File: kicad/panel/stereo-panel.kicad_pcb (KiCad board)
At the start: 2 copper layers, 144.1 x 144.1 mm, 347 parts, among them J1 AC IN 12-15V, J1 DC 12V IN, J1 IN L-G-R, J2 DC IN 12V, J2 IN L-G-R, J2 OUT L-G-R, J3 DC OUT 1, J3 LED IN, J3 SPK L, J4 DC OUT 2, J4 SPK R, J5 LED REMOTE, Q1 BC547, Q1001 BC547, Q1002 BC547, Q1003 BC557, Q1004 BD139, Q1005 BD140, Q1006 BC547, Q2 TIP41C, Q2001 BC547, Q2002 BC547, Q2003 BC557, Q2004 BD139, Q2005 BD140, Q2006 BC547, Q3 BC547

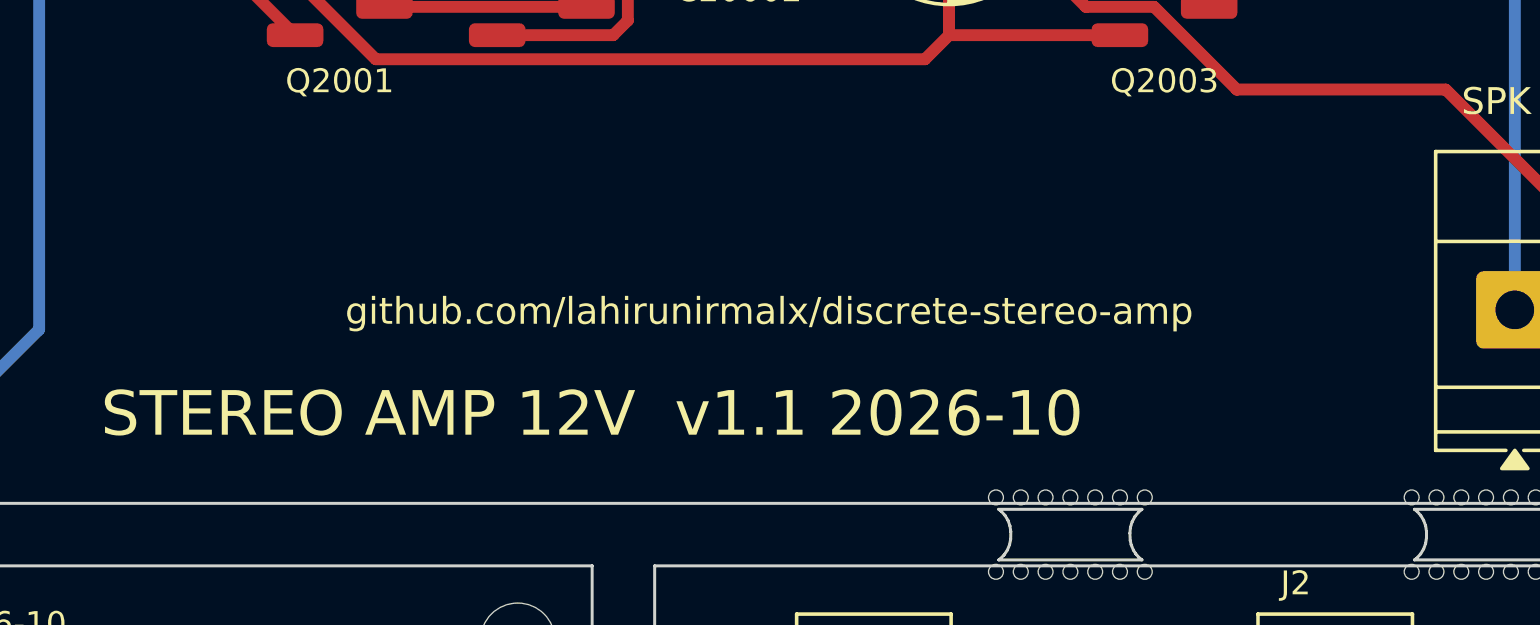
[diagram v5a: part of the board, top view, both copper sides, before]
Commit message: Compact 100 x 85 mm amp layout as a selectable second variant; modular build paths and the three design rules documented; per-board gerbers include both amps
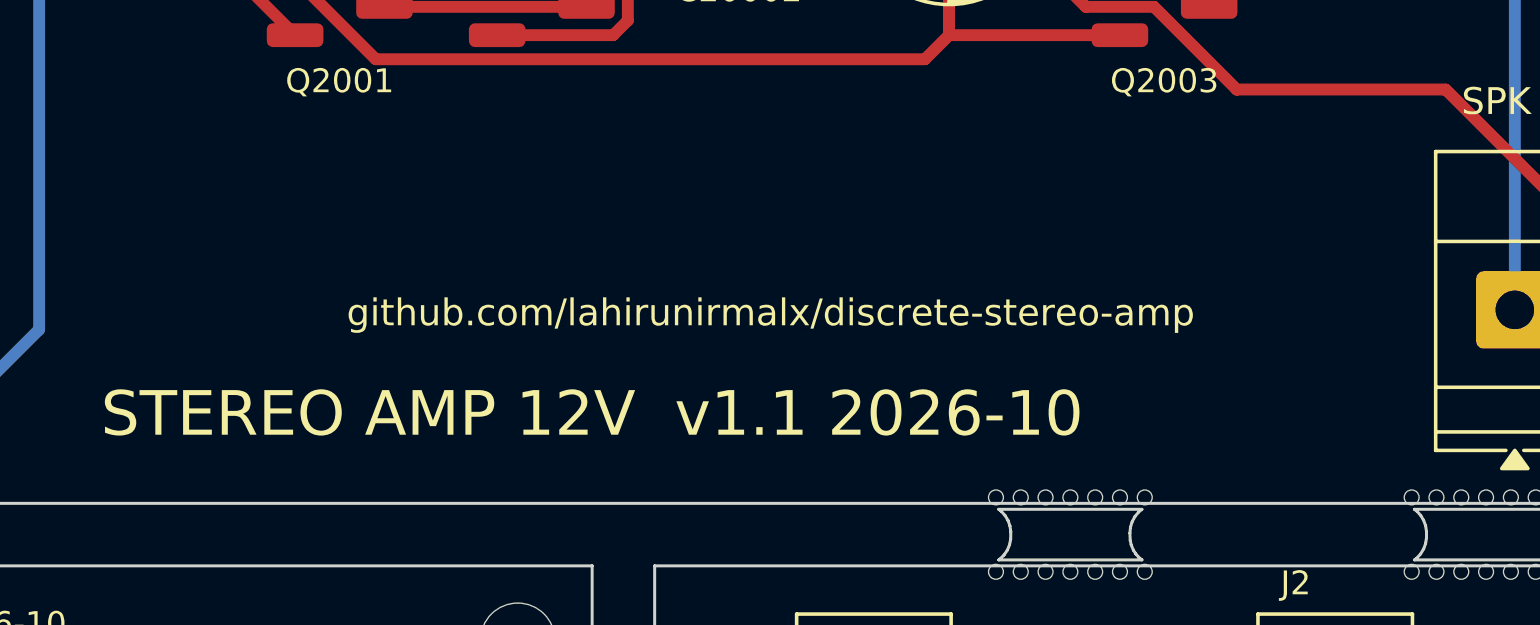
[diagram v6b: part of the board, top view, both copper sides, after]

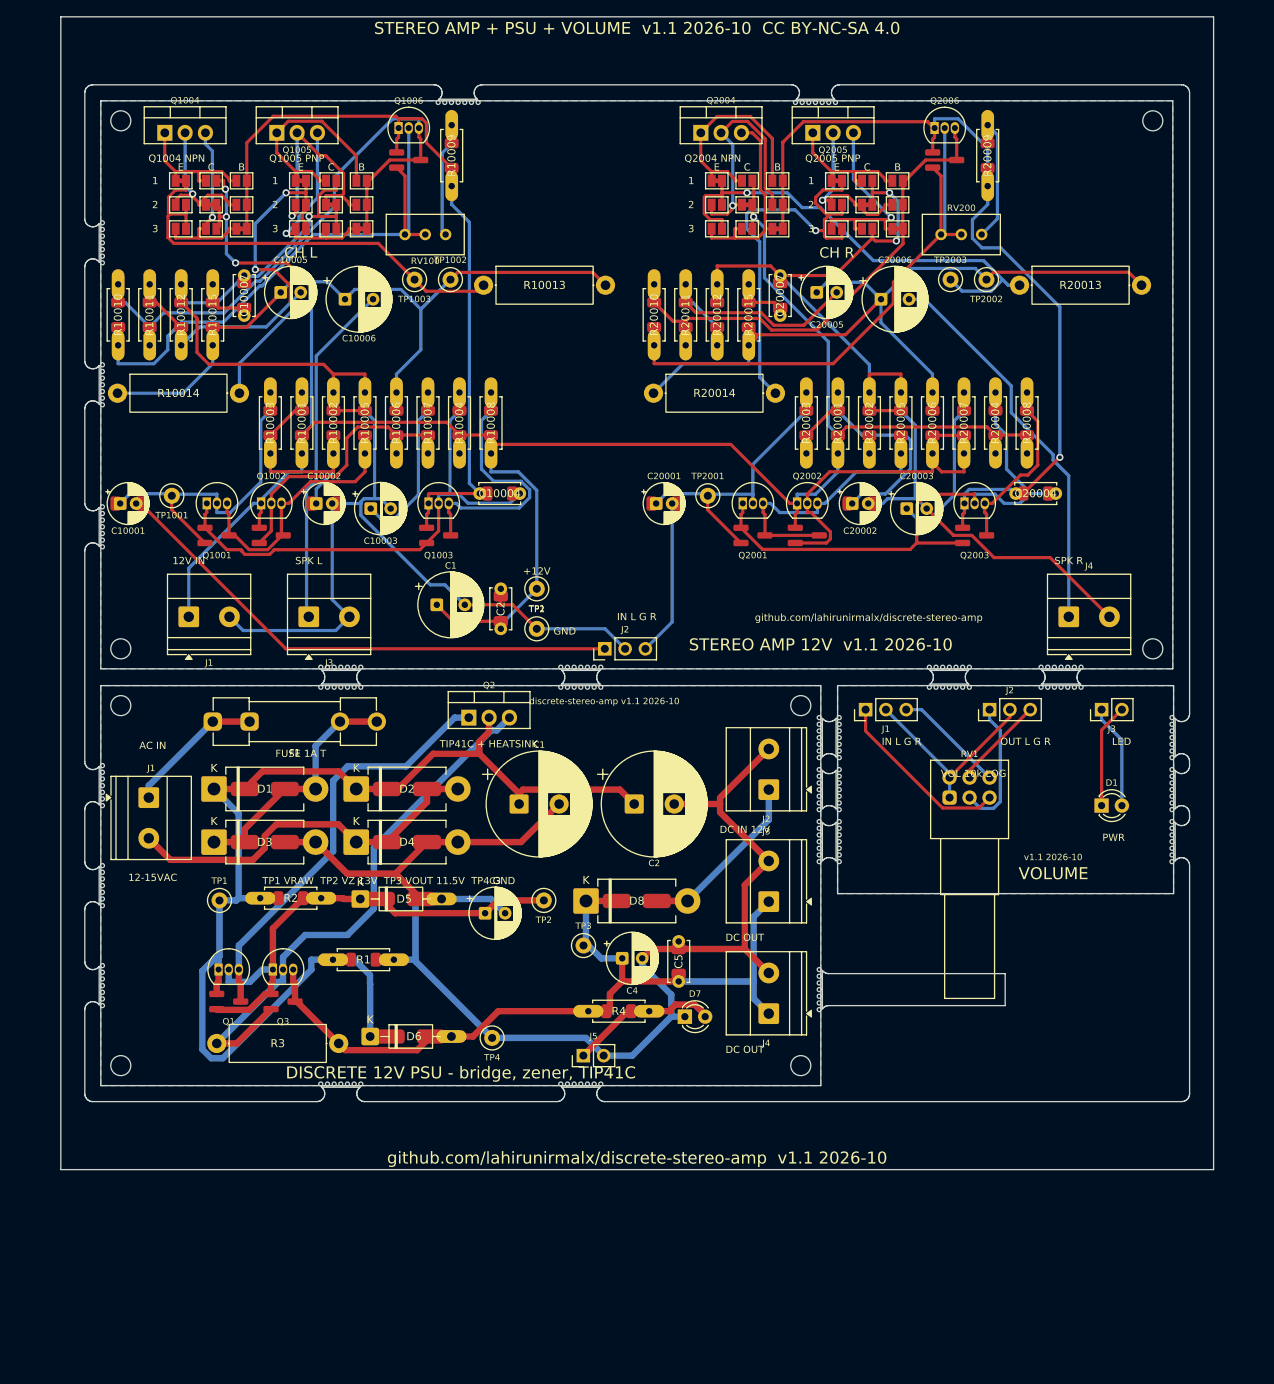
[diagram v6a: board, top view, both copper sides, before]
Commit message: Release 1.2: mirror-loaded front end, closed-loop PSU, VU tap, headphone board
- Amp: PNP input pair with NPN current-mirror load, LED-referenced current-source tail,
  NPN VAS with bootstrapped load from +12V, 220p Miller + 47p lead cap (THD 0.004% at 26 mW/8R,
  0.019% at 0.29 W; was 0.03 / 0.2). 1k VU meter tap per channel to header J5.
- PSU: BC547 error amplifier, 5.6 V zener fed from VOUT, 8.2k + 2k trimmer / 10k divider,
  2.2k drive, 47n/100n compensation. 12.0 V set point, 0.14 V dip on a 1 A step.
- New headphone board (DPDT switch, 120R series, DIRECT jumpers, 3.5 mm jack, panel-jack header).
- Boards: amp 134x85 / compact 100x98, PSU 90x58, hp 42x30; panel 155x155 with four boards.
  All 2-layer boards and the panel DRC clean; single-sided amp down to 15 errors.
- Toolchain: STAMP constant, reroute.sh second routing pass, rotated titles, link holes on
  jumper pads, 2 mm routing corridor per channel.
- Docs, BOMs, order guide, changelog, known issues rewritten for release 2.
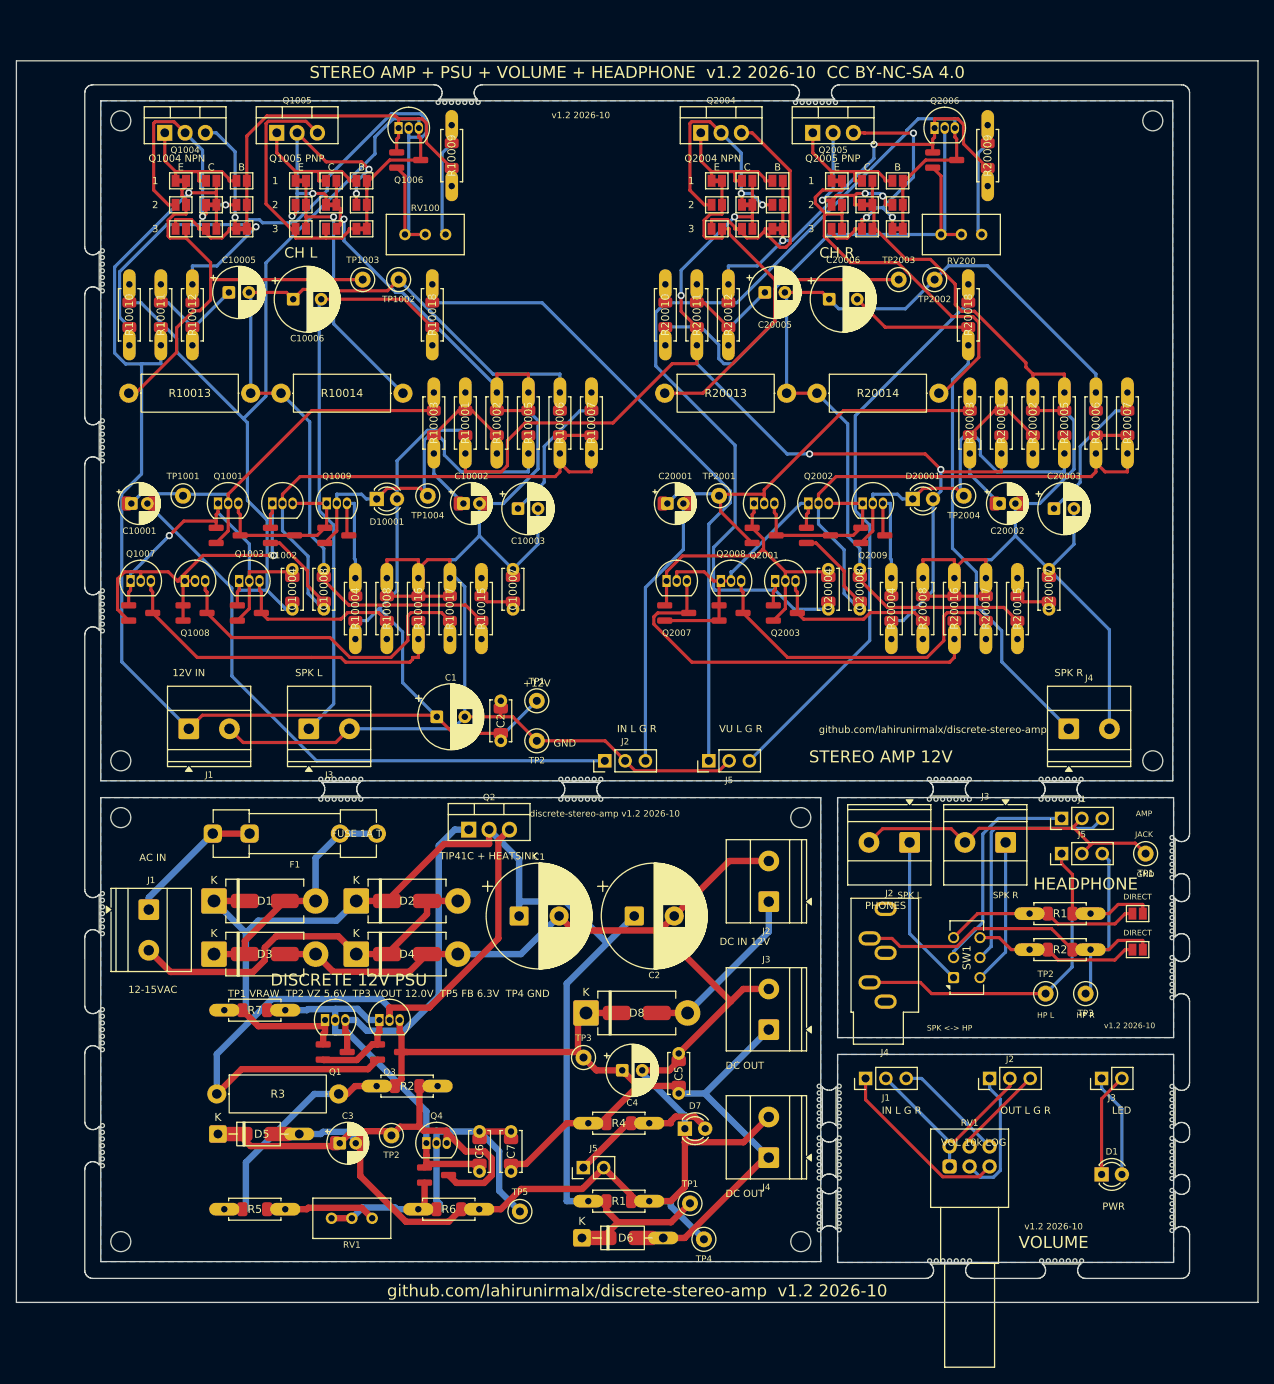
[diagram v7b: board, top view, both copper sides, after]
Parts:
- removed the C1 at (42.0, 63.0)
- removed the C1 at (52.3, 87.9)
- removed the C2 at (50.0, 66.0)
- removed the C2 at (66.7, 87.9)
- removed the D1 at (14.2, 86.0)
- removed the D1 at (125.1, 88.1)
- removed the H3 at (2.50, 68.5)
- removed the H3 at (2.50, 120.6)
- removed the H4 at (131.5, 68.5)
- removed the H4 at (87.5, 120.6)
- removed the J1 at (6.00, 87.1)
- removed the J1 at (95.6, 76.1)
- removed the J1 at (11.0, 64.5)
- removed the J2 at (63.0, 68.5)
- removed the J2 at (83.5, 86.1)
- removed the J2 at (111.1, 76.1)
- removed the J3 at (26.0, 64.5)
- removed the J3 at (125.1, 76.1)
- removed the J3 at (83.5, 100.1)
- removed the J4 at (83.5, 114.1)
- removed the J4 at (121.0, 64.5)
- removed the J5 at (60.3, 119.3)
- removed the R1 at (29.0, 107.4)
- removed the R2 at (19.9, 99.7)
- removed the RV1 at (106.1, 87.1)
- removed the TP1 at (54.5, 61.0)
- removed the TP1 at (14.8, 100.0)
- removed the TP2 at (54.5, 66.0)
- removed the TP2 at (55.4, 100.0)
- removed the TP3 at (60.3, 105.6)
- added C1: 1000u, Capacitor_THT:CP_Radial_D8.0mm_P3.50mm, F.Cu at (42.0, 77.0)
- added C1: 2200u, Capacitor_THT:CP_Radial_D13.0mm_P5.00mm, F.Cu at (52.3, 101.9)
- added C10008: 47p, Custom:C_P5_1206, F.Cu at (27.9, 63.6)
- added C2: 100n, Custom:C_P5_1206, F.Cu at (50.0, 80.0)
- added C2: 2200u, Capacitor_THT:CP_Radial_D13.0mm_P5.00mm, F.Cu at (66.7, 101.9)
- added C20008: 47p, Custom:C_P5_1206, F.Cu at (94.9, 63.6)
- added C6: 47n, Custom:C_P5_1206, F.Cu at (47.3, 133.8)
- added C7: 100n, Custom:C_P5_1206, F.Cu at (51.3, 133.8)
- added D1: POWER LED, LED_THT:LED_D3.0mm, F.Cu at (125.1, 134.2)
- added D1: 1N5401, Custom:D_DO201_SMA, F.Cu at (14.2, 100.0)
- added D10001: LED red, LED_THT:LED_D3.0mm, F.Cu at (34.5, 49.8)
- added D20001: LED red, LED_THT:LED_D3.0mm, F.Cu at (101.5, 49.8)
- added H3: M2.5, Custom:Hole_2.5mm, F.Cu at (2.50, 142.6)
- added H3: M2.5, Custom:Hole_2.5mm, F.Cu at (2.50, 82.5)
- added H4: M2.5, Custom:Hole_2.5mm, F.Cu at (131.5, 82.5)
- added H4: M2.5, Custom:Hole_2.5mm, F.Cu at (87.5, 142.6)
- added J1: AC IN 12-15V, TerminalBlock_Phoenix:TerminalBlock_Phoenix_MKDS-1,5-2-5.08_1x02_P5.08mm_Horizontal, F.Cu at (6.00, 101.1)
- added J1: IN L-G-R, Connector_PinHeader_2.54mm:PinHeader_1x03_P2.54mm_Vertical, F.Cu at (95.6, 122.2)
- added J1: DC 12V IN, TerminalBlock_Phoenix:TerminalBlock_Phoenix_MKDS-1,5-2-5.08_1x02_P5.08mm_Horizontal, F.Cu at (11.0, 78.5)
- added J1: FROM AMP L-G-R, Connector_PinHeader_2.54mm:PinHeader_1x03_P2.54mm_Vertical, F.Cu at (120.1, 89.7)
- added J2: IN L-G-R, Connector_PinHeader_2.54mm:PinHeader_1x03_P2.54mm_Vertical, F.Cu at (63.0, 82.5)
- added J2: DC IN 12V, TerminalBlock_Phoenix:TerminalBlock_Phoenix_MKDS-1,5-2-5.08_1x02_P5.08mm_Horizontal, F.Cu at (83.5, 100.1)
- added J2: SPK L, TerminalBlock_Phoenix:TerminalBlock_Phoenix_MKDS-1,5-2-5.08_1x02_P5.08mm_Horizontal, F.Cu at (101.1, 92.7)
- added J2: OUT L-G-R, Connector_PinHeader_2.54mm:PinHeader_1x03_P2.54mm_Vertical, F.Cu at (111.1, 122.2)
- added J3: SPK R, TerminalBlock_Phoenix:TerminalBlock_Phoenix_MKDS-1,5-2-5.08_1x02_P5.08mm_Horizontal, F.Cu at (113.1, 92.7)
- added J3: LED IN, Connector_PinHeader_2.54mm:PinHeader_1x02_P2.54mm_Vertical, F.Cu at (125.1, 122.2)
- added J3: SPK L, TerminalBlock_Phoenix:TerminalBlock_Phoenix_MKDS-1,5-2-5.08_1x02_P5.08mm_Horizontal, F.Cu at (26.0, 78.5)
- added J3: DC OUT 1, TerminalBlock_Phoenix:TerminalBlock_Phoenix_MKDS-1,5-2-5.08_1x02_P5.08mm_Horizontal, F.Cu at (83.5, 116.1)
- added J4: SPK R, TerminalBlock_Phoenix:TerminalBlock_Phoenix_MKDS-1,5-2-5.08_1x02_P5.08mm_Horizontal, F.Cu at (121.0, 78.5)
- added J4: 3.5mm TRS, Connector_Audio:Jack_3.5mm_CUI_SJ1-3535NG_Horizontal, F.Cu at (98.1, 112.6)
- added J4: DC OUT 2, TerminalBlock_Phoenix:TerminalBlock_Phoenix_MKDS-1,5-2-5.08_1x02_P5.08mm_Horizontal, F.Cu at (83.5, 132.1)
- added J5: LED REMOTE, Connector_PinHeader_2.54mm:PinHeader_1x02_P2.54mm_Vertical, F.Cu at (60.3, 133.3)
- added J5: PANEL JACK T-G-R, Connector_PinHeader_2.54mm:PinHeader_1x03_P2.54mm_Vertical, F.Cu at (120.1, 94.1)
- added J5: VU L-G-R, Connector_PinHeader_2.54mm:PinHeader_1x03_P2.54mm_Vertical, F.Cu at (76.0, 82.5)
- added JP1: DIRECT, Jumper:SolderJumper-2_P1.3mm_Open_Pad1.0x1.5mm, F.Cu at (129.6, 101.6)
- added JP2: DIRECT, Jumper:SolderJumper-2_P1.3mm_Open_Pad1.0x1.5mm, F.Cu at (129.6, 106.1)
- added KiKit_MB_29_1: NPTH, NPTH, F.Cu at (108.6, 145.0)
- added KiKit_MB_29_2: NPTH, NPTH, F.Cu at (107.8, 145.0)
- added KiKit_MB_29_3: NPTH, NPTH, F.Cu at (106.9, 145.0)
- added KiKit_MB_29_4: NPTH, NPTH, F.Cu at (106.1, 145.0)
- added KiKit_MB_29_5: NPTH, NPTH, F.Cu at (105.3, 145.0)
- added KiKit_MB_29_6: NPTH, NPTH, F.Cu at (104.4, 145.0)
- added KiKit_MB_29_7: NPTH, NPTH, F.Cu at (103.6, 145.0)
- added KiKit_MB_30_1: NPTH, NPTH, F.Cu at (122.6, 145.0)
- added KiKit_MB_30_2: NPTH, NPTH, F.Cu at (121.8, 145.0)
- added KiKit_MB_30_3: NPTH, NPTH, F.Cu at (120.9, 145.0)
- added KiKit_MB_30_4: NPTH, NPTH, F.Cu at (120.1, 145.0)
- added KiKit_MB_30_5: NPTH, NPTH, F.Cu at (119.3, 145.0)
- added KiKit_MB_30_6: NPTH, NPTH, F.Cu at (118.4, 145.0)
- added KiKit_MB_30_7: NPTH, NPTH, F.Cu at (117.6, 145.0)
- added Q1007: BC547, Custom:TO92_SOT23, F.Cu at (3.72, 60.0)
- added Q1008: BC547, Custom:TO92_SOT23, F.Cu at (10.5, 60.0)
- added Q1009: BC557, Custom:TO92_SOT23, F.Cu at (28.2, 50.3)
- added Q2007: BC547, Custom:TO92_SOT23, F.Cu at (70.7, 60.0)
- added Q2008: BC547, Custom:TO92_SOT23, F.Cu at (77.5, 60.0)
- added Q2009: BC557, Custom:TO92_SOT23, F.Cu at (95.2, 50.3)
- added Q4: BC547, Custom:TO92_SOT23, F.Cu at (40.7, 130.3)
- added R1: 120, Custom:R_Axial_1206, F.Cu at (116.1, 101.6)
- added R1: 4.7k, Custom:R_Axial_1206, F.Cu at (60.9, 137.5)
- added R10016: 100, Custom:R_Axial_1206, F.Cu at (39.7, 67.3)
- added R10017: 100, Custom:R_Axial_1206, F.Cu at (43.6, 67.3)
- added R10018: 1k, Custom:R_Axial_1206, F.Cu at (41.4, 30.6)
- added R2: 1k, Custom:R_Axial_1206, F.Cu at (34.5, 123.2)
- added R2: 120, Custom:R_Axial_1206, F.Cu at (116.1, 106.1)
- added R20016: 100, Custom:R_Axial_1206, F.Cu at (106.7, 67.3)
- added R20017: 100, Custom:R_Axial_1206, F.Cu at (110.6, 67.3)
- added R20018: 1k, Custom:R_Axial_1206, F.Cu at (108.4, 30.6)
- added R5: 8.2k, Custom:R_Axial_1206, F.Cu at (15.4, 138.6)
- added R6: 10k, Custom:R_Axial_1206, F.Cu at (39.7, 138.6)
- added R7: 2.2k, Custom:R_Axial_1206, F.Cu at (15.4, 113.7)
- added RV1: 10k log dual, Potentiometer_THT:Potentiometer_Alps_RK097_Dual_Horizontal, F.Cu at (106.1, 133.2)
- added RV1: 2k, Potentiometer_THT:Potentiometer_Bourns_3296W_Vertical, F.Cu at (33.9, 139.7)
- added SW1: SPK / HP, Button_Switch_THT:SW_CK_JS202011CQN_DPDT_Straight, F.Cu at (106.6, 109.6)
- added TP1: +12V, TestPoint:TestPoint_Loop_D2.50mm_Drill1.0mm, F.Cu at (54.5, 75.0)
- added TP1: GND, TestPoint:TestPoint_Loop_D2.50mm_Drill1.0mm, F.Cu at (130.6, 94.1)
- added TP1: VRAW 14-19V, TestPoint:TestPoint_Loop_D2.50mm_Drill1.0mm, F.Cu at (73.7, 137.8)
- added TP1004: LED 10.2V, TestPoint:TestPoint_Loop_D2.50mm_Drill1.0mm, F.Cu at (40.9, 49.4)
- added TP2: VZ 5.6V, TestPoint:TestPoint_Loop_D2.50mm_Drill1.0mm, F.Cu at (36.3, 129.3)
- added TP2: HP L, TestPoint:TestPoint_Loop_D2.50mm_Drill1.0mm, F.Cu at (118.1, 111.6)
- added TP2: GND, TestPoint:TestPoint_Loop_D2.50mm_Drill1.0mm, F.Cu at (54.5, 80.0)
- added TP2004: LED 10.2V, TestPoint:TestPoint_Loop_D2.50mm_Drill1.0mm, F.Cu at (107.9, 49.4)
- added TP3: HP R, TestPoint:TestPoint_Loop_D2.50mm_Drill1.0mm, F.Cu at (123.1, 111.6)
- added TP3: VOUT 12.0V, TestPoint:TestPoint_Loop_D2.50mm_Drill1.0mm, F.Cu at (60.3, 119.6)
- added TP5: FB 6.3V, TestPoint:TestPoint_Loop_D2.50mm_Drill1.0mm, F.Cu at (52.4, 138.8)
- C10004, C20004: value 100p -> 220p
- C3: value 100u -> 10u; footprint Capacitor_THT:CP_Radial_D6.3mm_P2.50mm -> Custom:CE_P2_1206
- D5: value 13V 1W -> 5.6V
- Q1001, Q1002, Q2001, Q2002: value BC547 -> BC557
- Q1003, Q2003: value BC557 -> BC547
- R10004, R20004: value 4.7k -> 1.2k
- R10005, R20005: value 10k -> 4.7k
- TP1001, TP2001: value B1 5.9V -> B1 6.1V
- moved KiKit_MB_19_7 108.0 mm to (133.9, 104.6)
- moved KiKit_MB_19_6 107.3 mm to (133.9, 103.8)
- moved KiKit_MB_19_5 106.6 mm to (133.9, 102.9)
- moved KiKit_MB_19_4 106.0 mm to (133.9, 102.1)
- moved KiKit_MB_19_3 105.3 mm to (133.9, 101.3)
- moved KiKit_MB_19_2 104.7 mm to (133.9, 100.4)
- moved KiKit_MB_19_1 104.0 mm to (133.9, 99.6)
- moved KiKit_MB_18_1 78.7 mm to (133.9, 92.1)
- moved KiKit_MB_18_2 78.1 mm to (133.9, 92.9)
- moved KiKit_MB_18_3 77.5 mm to (133.9, 93.8)
- moved KiKit_MB_20_7 77.2 mm to (133.9, 112.1)
- moved KiKit_MB_18_4 76.9 mm to (133.9, 94.6)
- moved KiKit_MB_20_6 76.5 mm to (133.9, 111.3)
- moved KiKit_MB_18_5 76.3 mm to (133.9, 95.4)
- moved KiKit_MB_18_6 75.8 mm to (133.9, 96.3)
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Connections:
- C10004 pad 1: Board_0-/VAS_L -> Board_0-/B5_L
- C10004 pad 1S: Board_0-/VAS_L -> Board_0-/B5_L
- C10005 pad 1: Board_0-/OUT_L -> Board_0-Net-(C10005-Pad1)
- C10005 pad 2: Board_0-Net-(C10005-Pad2) -> Board_0-/OUT_L
- C20004 pad 1: Board_0-/VAS_R -> Board_0-/B5_R
- C20004 pad 1S: Board_0-/VAS_R -> Board_0-/B5_R
- C20005 pad 1: Board_0-/OUT_R -> Board_0-Net-(C20005-Pad1)
- C20005 pad 2: Board_0-Net-(C20005-Pad2) -> Board_0-/OUT_R
- C3 pad 1: Board_1-/VZ -> Board_1-Net-(D5-K)
- D5 pad 1: Board_1-/VZ -> Board_1-Net-(D5-K)
- D5 pad 1S: Board_1-/VZ -> Board_1-Net-(D5-K)
- Q1 pad 2: Board_1-/VZ -> Board_1-/BQ1
- Q1 pad 2S: Board_1-/VZ -> Board_1-/BQ1
- Q1002 pad 1: Board_0-+12V -> Board_0-Net-(Q1002-C)
- Q1002 pad 1S: Board_0-+12V -> Board_0-Net-(Q1002-C)
- Q1003 pad 1: Board_0-/VAS_L -> Board_0-/B5_L
- Q1003 pad 1S: Board_0-/VAS_L -> Board_0-/B5_L
- Q2002 pad 1: Board_0-+12V -> Board_0-Net-(Q2002-C)
- Q2002 pad 1S: Board_0-+12V -> Board_0-Net-(Q2002-C)
- Q2003 pad 1: Board_0-/VAS_R -> Board_0-/B5_R
- Q2003 pad 1S: Board_0-/VAS_R -> Board_0-/B5_R
- Q3 pad 1: Board_1-/VZ -> Board_1-/BQ1
- Q3 pad 1S: Board_1-/VZ -> Board_1-/BQ1
- R10004 pad 2: Board_0-Net-(Q1001-C) -> Board_0-Net-(Q1009-E)
- R10004 pad 2S: Board_0-Net-(Q1001-C) -> Board_0-Net-(Q1009-E)
- R10005 pad 1: Board_0-Net-(Q1001-E) -> Board_0-Net-(D10001-K)
- R10005 pad 1S: Board_0-Net-(Q1001-E) -> Board_0-Net-(D10001-K)
- R10008 pad 1: Board_0-+12V -> Board_0-Net-(Q1003-E)
- R10008 pad 1S: Board_0-+12V -> Board_0-Net-(Q1003-E)
- R10008 pad 2: Board_0-Net-(Q1003-E) -> Board_0-GND
- R10008 pad 2S: Board_0-Net-(Q1003-E) -> Board_0-GND
- R10011 pad 1: Board_0-/B5_L -> Board_0-+12V
- R10011 pad 1S: Board_0-/B5_L -> Board_0-+12V
- R10011 pad 2: Board_0-Net-(C10005-Pad2) -> Board_0-Net-(C10005-Pad1)
- R10011 pad 2S: Board_0-Net-(C10005-Pad2) -> Board_0-Net-(C10005-Pad1)
- R10012 pad 1: Board_0-Net-(C10005-Pad2) -> Board_0-Net-(C10005-Pad1)
- R10012 pad 1S: Board_0-Net-(C10005-Pad2) -> Board_0-Net-(C10005-Pad1)
- R10012 pad 2: Board_0-GND -> Board_0-/VAS_L
- R10012 pad 2S: Board_0-GND -> Board_0-/VAS_L
- R20004 pad 2: Board_0-Net-(Q2001-C) -> Board_0-Net-(Q2009-E)
- R20004 pad 2S: Board_0-Net-(Q2001-C) -> Board_0-Net-(Q2009-E)
- R20005 pad 1: Board_0-Net-(Q2001-E) -> Board_0-Net-(D20001-K)
- R20005 pad 1S: Board_0-Net-(Q2001-E) -> Board_0-Net-(D20001-K)
- R20008 pad 1: Board_0-+12V -> Board_0-Net-(Q2003-E)
- R20008 pad 1S: Board_0-+12V -> Board_0-Net-(Q2003-E)
- R20008 pad 2: Board_0-Net-(Q2003-E) -> Board_0-GND
- R20008 pad 2S: Board_0-Net-(Q2003-E) -> Board_0-GND
- R20011 pad 1: Board_0-/B5_R -> Board_0-+12V
- R20011 pad 1S: Board_0-/B5_R -> Board_0-+12V
- R20011 pad 2: Board_0-Net-(C20005-Pad2) -> Board_0-Net-(C20005-Pad1)
- R20011 pad 2S: Board_0-Net-(C20005-Pad2) -> Board_0-Net-(C20005-Pad1)
- R20012 pad 1: Board_0-Net-(C20005-Pad2) -> Board_0-Net-(C20005-Pad1)
- R20012 pad 1S: Board_0-Net-(C20005-Pad2) -> Board_0-Net-(C20005-Pad1)
- R20012 pad 2: Board_0-GND -> Board_0-/VAS_R
- R20012 pad 2S: Board_0-GND -> Board_0-/VAS_R
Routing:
- net Board_0-/VU_L: track 0.00 -> 86.4 mm
- net Board_0-/VU_R: track 0.00 -> 74.6 mm
- net Board_0-+12V: track 274.7 -> 348.0 mm
- net Board_0-/B5_R: track 63.3 -> 132.5 mm
- net Board_1-/VZ: track 60.5 -> 0.00 mm
- net Board_2-/JACK_R: track 0.00 -> 58.6 mm
- net Board_1-/BQ1: track 0.00 -> 58.5 mm
- net Board_1-Net-(D5-K): track 0.00 -> 55.1 mm
- net Board_2-/JACK_L: track 0.00 -> 54.7 mm
- net Board_0-Net-(Q2007-E): track 0.00 -> 53.9 mm
- net Board_1-Net-(Q4-B): track 0.00 -> 53.1 mm
- net Board_0-GND: track 305.2 -> 357.9 mm, vias 3 -> 1
- net Board_1-Net-(D6-A): track 103.0 -> 155.7 mm
- net Board_0-/B5_L: track 80.9 -> 129.8 mm
- net Board_0-/VAS_R: track 109.8 -> 62.1 mm, vias 1 -> 2
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- added copper zone on B.Cu, net Board_3-GND
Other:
- board size 144.1 x 144.1 mm -> 155.2 x 155.2 mm
- board text added: "AMP"
- board text added: "DIRECT"
- board text added: "DISCRETE 12V PSU"
- board text added: "HEADPHONE"
- board text added: "HP L"
- board text added: "HP R"
- board text added: "JACK"
- board text added: "PHONES"
- board text added: "SPK <-> HP"
- board text added: "STEREO AMP + PSU + VOLUME + HEADPHONE v1.2 2026-10 CC BY-NC-SA 4.0"
- board text added: "STEREO AMP 12V"
- board text added: "TP1 VRAW TP2 VZ 5.6V TP3 VOUT 12.0V TP5 FB 6.3V TP4 GND"
- board text added: "VU L G R"
- board text added: "discrete-stereo-amp v1.2 2026-10"
- board text added: "github.com/lahirunirmalx/discrete-stereo-amp v1.2 2026-10"
- board text added: "v1.2 2026-10"
- board text removed: "DISCRETE 12V PSU - bridge, zener, TIP41C"
- board text removed: "STEREO AMP + PSU + VOLUME v1.1 2026-10 CC BY-NC-SA 4.0"
- board text removed: "STEREO AMP 12V v1.1 2026-10"
- board text removed: "TP1 VRAW TP2 VZ 13V TP3 VOUT 11.5V TP4 GND"
- board text removed: "discrete-stereo-amp v1.1 2026-10"
- board text removed: "github.com/lahirunirmalx/discrete-stereo-amp v1.1 2026-10"
- board text removed: "v1.1 2026-10"
